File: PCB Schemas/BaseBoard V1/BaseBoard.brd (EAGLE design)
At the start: 94 x 31.1 mm, 31 parts, among them IC1 74HC595D, IC2 74HC595D, IC3 74HC595D, U1 ATMEGA2560AU, X1 16MHz

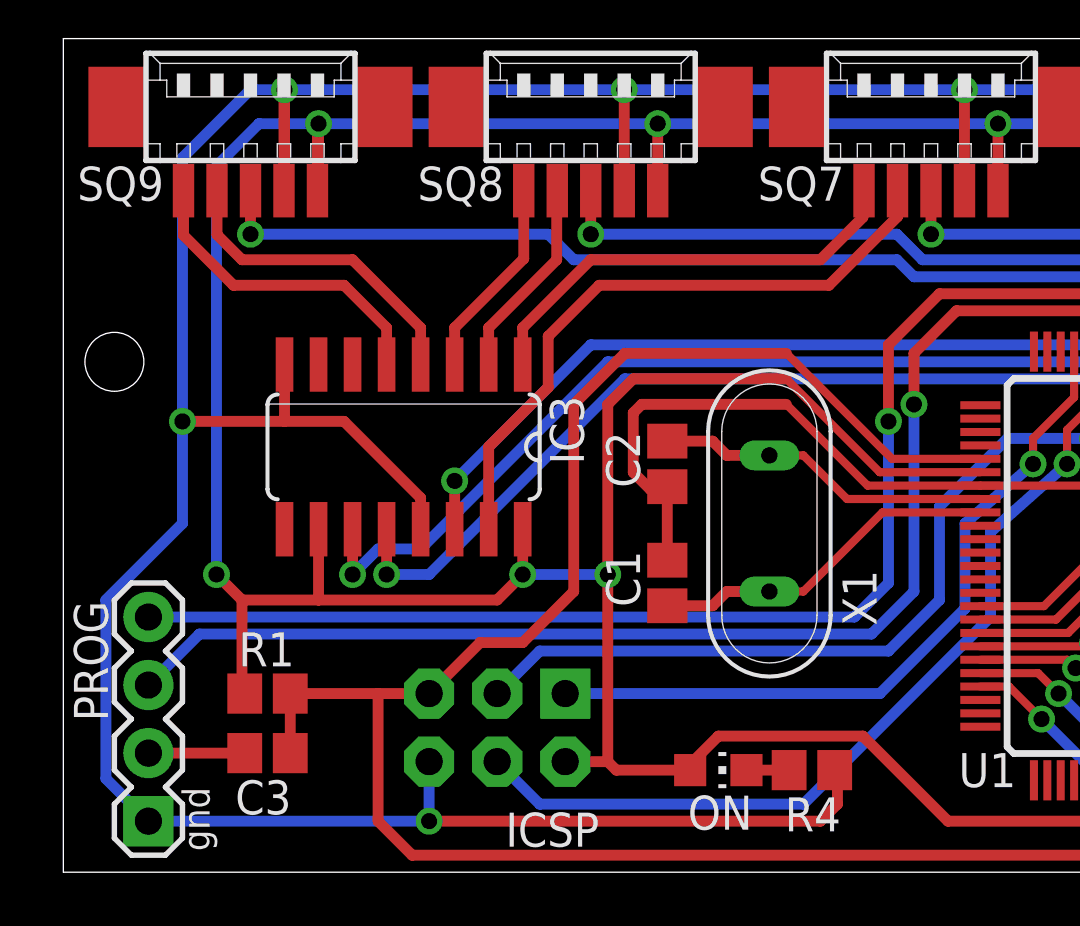
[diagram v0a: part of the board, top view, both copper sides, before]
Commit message: Corrected BaseBoard V1 and updated license file
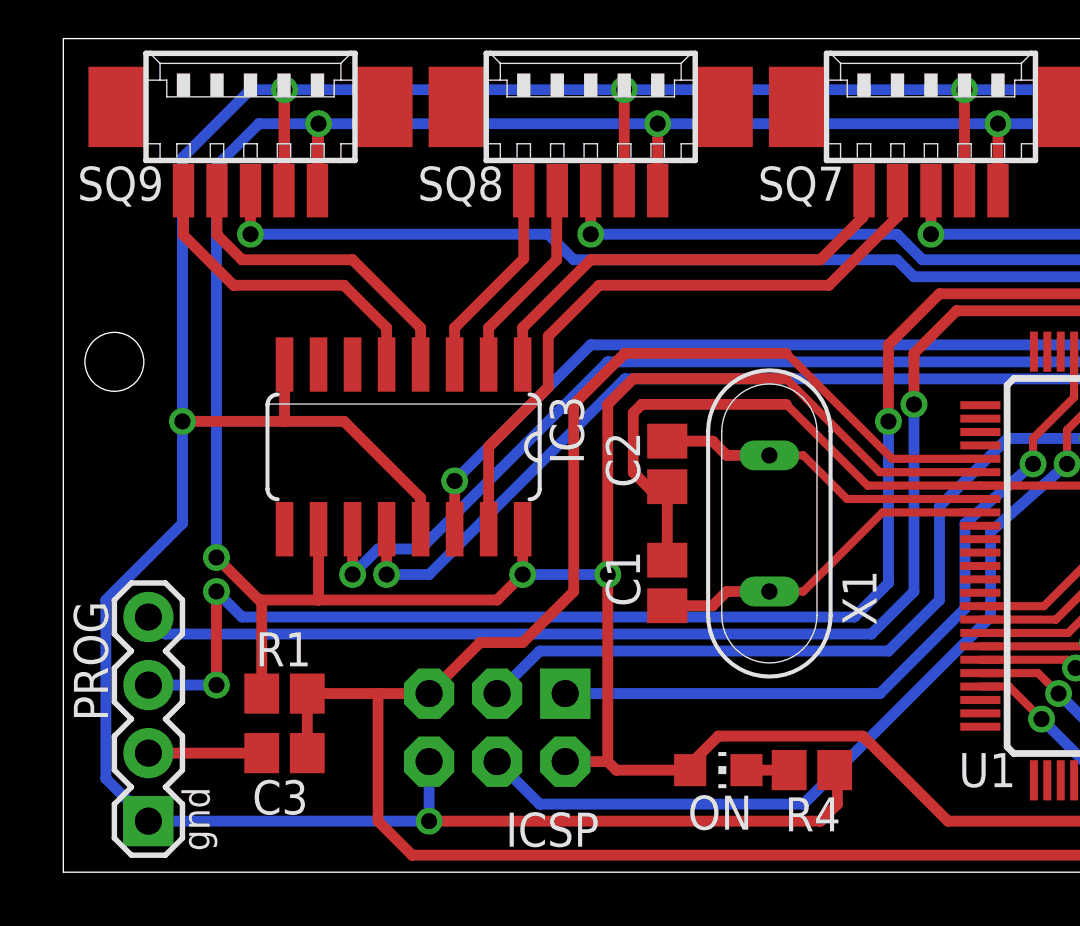
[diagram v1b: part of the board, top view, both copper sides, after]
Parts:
- moved C3 0.64 mm to (8.26, 4.45)
- moved R1 0.64 mm to (8.26, 6.67)
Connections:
- net RX: now also PROG.3; no longer PROG.4
- net TX: now also PROG.4; no longer PROG.3
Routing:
- net RX: track 56.5 -> 60.4 mm, vias 1 -> 3
- net RESET: track 100.3 -> 99.7 mm
- net N$5: track 3.59 -> 4.23 mm
- net TX: track 56.2 -> 55.7 mm
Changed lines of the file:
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@@
 <attribute name="VALUE" x="38.4175" y="16.51" size="0.4064" layer="27" rot="R270"/>
 </element>
-<element name="R1" library="resistor" package="R0805" value="10k" x="7.62" y="6.6675" smashed="yes" rot="R180">
-<attribute name="NAME" x="6.5405" y="7.6835" size="1.27" layer="25"/>
-<attribute name="VALUE" x="8.382" y="8.9535" size="1.27" layer="27" rot="R180"/>
+<element name="R1" library="resistor" package="R0805" value="10k" x="8.255" y="6.6675" smashed="yes" rot="R180">
+<attribute name="NAME" x="7.1755" y="7.6835" size="1.27" layer="25"/>
+<attribute name="VALUE" x="9.017" y="8.9535" size="1.27" layer="27" rot="R180"/>
 </element>
 <element name="X1" library="special" package="QS" value="16MHz" x="26.3525" y="13.0175" smashed="yes" rot="R90">
@@
 <attribute name="VALUE" x="6.35" y="0.635" size="1.27" layer="27" rot="R90"/>
 </element>
-<element name="C3" library="resistor" package="C0805" value="100nF" x="7.62" y="4.445" smashed="yes">
-<attribute name="NAME" x="8.509" y="3.429" size="1.27" layer="25" rot="R180"/>
-<attribute name="VALUE" x="6.731" y="2.159" size="1.27" layer="27"/>
+<element name="C3" library="resistor" package="C0805" value="100nF" x="8.255" y="4.445" smashed="yes">
+<attribute name="NAME" x="9.144" y="3.429" size="1.27" layer="25" rot="R180"/>
+<attribute name="VALUE" x="7.366" y="2.159" size="1.27" layer="27"/>
 </element>
 <element name="C4" library="resistor" package="C0805" value="100nF" x="54.2925" y="17.4625" rot="R270"/>
@@
 <via x="9.525" y="27.94" extent="1-16" drill="0.6"/>
 <wire x1="9.525" y1="27.94" x2="22.185" y2="27.94" width="0.4064" layer="16"/>
-<via x="5.715" y="11.1125" extent="1-16" drill="0.6"/>
-<wire x1="5.715" y1="11.1125" x2="5.715" y2="26.3525" width="0.4064" layer="16"/>
+<via x="5.715" y="11.7475" extent="1-16" drill="0.6"/>
+<wire x1="5.715" y1="11.7475" x2="5.715" y2="26.3525" width="0.4064" layer="16"/>
 <wire x1="5.715" y1="26.3525" x2="7.3025" y2="27.94" width="0.4064" layer="16"/>
 <wire x1="7.3025" y1="27.94" x2="9.525" y2="27.94" width="0.4064" layer="16"/>
 <wire x1="9.525" y1="10.16" x2="9.525" y2="12.8016" width="0.4064" layer="1"/>
-<wire x1="6.6675" y1="10.16" x2="9.525" y2="10.16" width="0.4064" layer="1"/>
-<wire x1="6.6675" y1="10.16" x2="6.6675" y2="6.77" width="0.4064" layer="1"/>
-<wire x1="6.6675" y1="6.77" x2="6.77" y2="6.6675" width="0.4064" layer="1"/>
 <wire x1="62.5475" y1="12.8016" x2="62.5475" y2="10.16" width="0.4064" layer="1"/>
 <wire x1="70.1675" y1="11.1125" x2="70.1675" y2="12.8016" width="0.4064" layer="1"/>
@@
 <wire x1="51.435" y1="17.78" x2="51.435" y2="20.0025" width="0.3048" layer="1"/>
 <wire x1="20.32" y1="4.1275" x2="18.7325" y2="4.1275" width="0.4064" layer="1"/>
-<wire x1="5.715" y1="11.1125" x2="6.6675" y2="10.16" width="0.4064" layer="1"/>
 <wire x1="9.525" y1="10.16" x2="16.1925" y2="10.16" width="0.4064" layer="1"/>
 <wire x1="17.145" y1="11.1125" x2="17.145" y2="12.8016" width="0.4064" layer="1"/>
@@
 <wire x1="71.04" y1="4.4925" x2="90.1775" y2="4.4925" width="0.4064" layer="16"/>
 <wire x1="90.1775" y1="4.4925" x2="90.805" y2="5.12" width="0.4064" layer="16"/>
+<wire x1="7.405" y1="6.6675" x2="7.405" y2="10.0575" width="0.4064" layer="1"/>
+<wire x1="7.405" y1="10.16" x2="7.405" y2="10.0575" width="0.4064" layer="1"/>
+<wire x1="7.405" y1="10.0575" x2="5.715" y2="11.7475" width="0.4064" layer="1"/>
+<wire x1="9.525" y1="10.16" x2="7.405" y2="10.16" width="0.4064" layer="1"/>
 </signal>
 <signal name="RESET">
@@
 <contactref element="C3" pad="2"/>
 <contactref element="ICSP" pad="5"/>
-<wire x1="8.47" y1="6.6675" x2="8.47" y2="4.445" width="0.4064" layer="1"/>
-<wire x1="8.47" y1="6.6675" x2="11.7475" y2="6.6675" width="0.4064" layer="1"/>
+<wire x1="9.105" y1="6.6675" x2="9.105" y2="4.445" width="0.4064" layer="1"/>
+<wire x1="9.105" y1="6.6675" x2="11.7475" y2="6.6675" width="0.4064" layer="1"/>
 <wire x1="11.7475" y1="6.6675" x2="13.6525" y2="6.6675" width="0.4064" layer="1"/>
 <wire x1="34.2275" y1="15.43" x2="30.925" y2="15.43" width="0.3048" layer="1"/>
@@
 </signal>
 <signal name="RX">
-<contactref element="PROG" pad="4"/>
 <contactref element="U1" pad="2"/>
 <wire x1="47.7275" y1="19.43" x2="47.7275" y2="20.8525" width="0.3048" layer="1"/>
@@
 <wire x1="46.99" y1="21.59" x2="32.7025" y2="21.59" width="0.4064" layer="1"/>
 <wire x1="32.7025" y1="21.59" x2="30.7975" y2="19.685" width="0.4064" layer="1"/>
-<wire x1="3.175" y1="9.525" x2="29.5275" y2="9.525" width="0.4064" layer="16"/>
-<wire x1="29.5275" y1="9.525" x2="30.7975" y2="10.795" width="0.4064" layer="16"/>
 <wire x1="30.7975" y1="10.795" x2="30.7975" y2="16.8275" width="0.4064" layer="16"/>
 <via x="30.7975" y="16.8275" extent="1-16" drill="0.6"/>
 <wire x1="30.7975" y1="19.685" x2="30.7975" y2="16.8275" width="0.4064" layer="1"/>
+<contactref element="PROG" pad="3"/>
+<wire x1="30.7975" y1="10.795" x2="29.5275" y2="9.525" width="0.4064" layer="16"/>
+<wire x1="29.5275" y1="9.525" x2="6.6675" y2="9.525" width="0.4064" layer="16"/>
+<wire x1="6.6675" y1="9.525" x2="5.715" y2="10.4775" width="0.4064" layer="16"/>
+<wire x1="3.175" y1="6.985" x2="5.715" y2="6.985" width="0.4064" layer="16"/>
+<via x="5.715" y="6.985" extent="1-16" drill="0.6"/>
+<via x="5.715" y="10.4775" extent="1-16" drill="0.6"/>
+<wire x1="5.715" y1="6.985" x2="5.715" y2="10.4775" width="0.4064" layer="1"/>
 </signal>
 <signal name="TX">
-<contactref element="PROG" pad="3"/>
 <contactref element="U1" pad="3"/>
 <wire x1="47.2275" y1="19.43" x2="47.2275" y2="20.4" width="0.3048" layer="1"/>
@@
 <wire x1="46.6725" y1="20.955" x2="33.3375" y2="20.955" width="0.4064" layer="1"/>
 <wire x1="33.3375" y1="20.955" x2="31.75" y2="19.3675" width="0.4064" layer="1"/>
-<wire x1="5.08" y1="8.89" x2="30.1625" y2="8.89" width="0.4064" layer="16"/>
-<wire x1="30.1625" y1="8.89" x2="31.75" y2="10.4775" width="0.4064" layer="16"/>
 <wire x1="31.75" y1="10.4775" x2="31.75" y2="17.4625" width="0.4064" layer="16"/>
 <via x="31.75" y="17.4625" extent="1-16" drill="0.6"/>
 <wire x1="31.75" y1="19.3675" x2="31.75" y2="17.4625" width="0.4064" layer="1"/>
-<wire x1="5.08" y1="8.89" x2="3.175" y2="6.985" width="0.4064" layer="16"/>
+<contactref element="PROG" pad="4"/>
+<wire x1="31.75" y1="10.4775" x2="30.1625" y2="8.89" width="0.4064" layer="16"/>
+<wire x1="30.1625" y1="8.89" x2="3.81" y2="8.89" width="0.4064" layer="16"/>
+<wire x1="3.81" y1="8.89" x2="3.175" y2="9.525" width="0.4064" layer="16"/>
 </signal>
 <signal name="N$5">
 <contactref element="PROG" pad="2"/>
 <contactref element="C3" pad="1"/>
-<wire x1="6.77" y1="4.445" x2="3.175" y2="4.445" width="0.4064" layer="1"/>
+<wire x1="7.405" y1="4.445" x2="3.175" y2="4.445" width="0.4064" layer="1"/>
 </signal>
 <signal name="AREF">

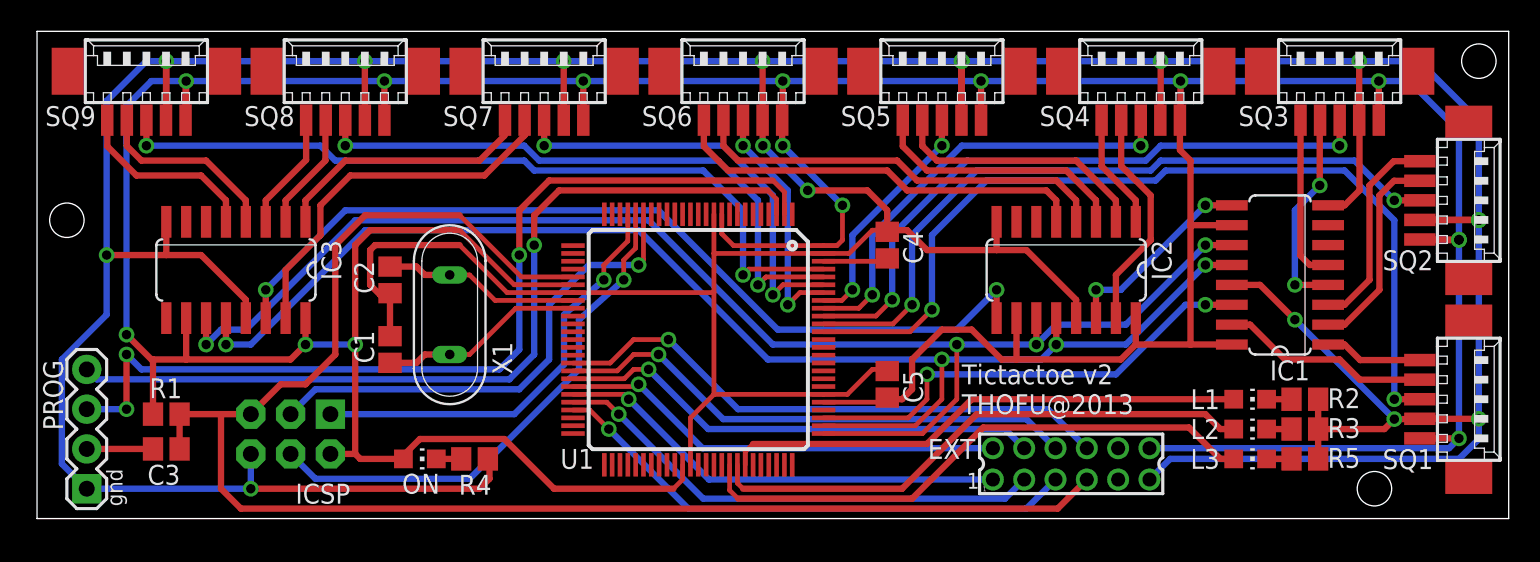
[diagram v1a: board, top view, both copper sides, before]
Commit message: Modified base conector; delete reset pin
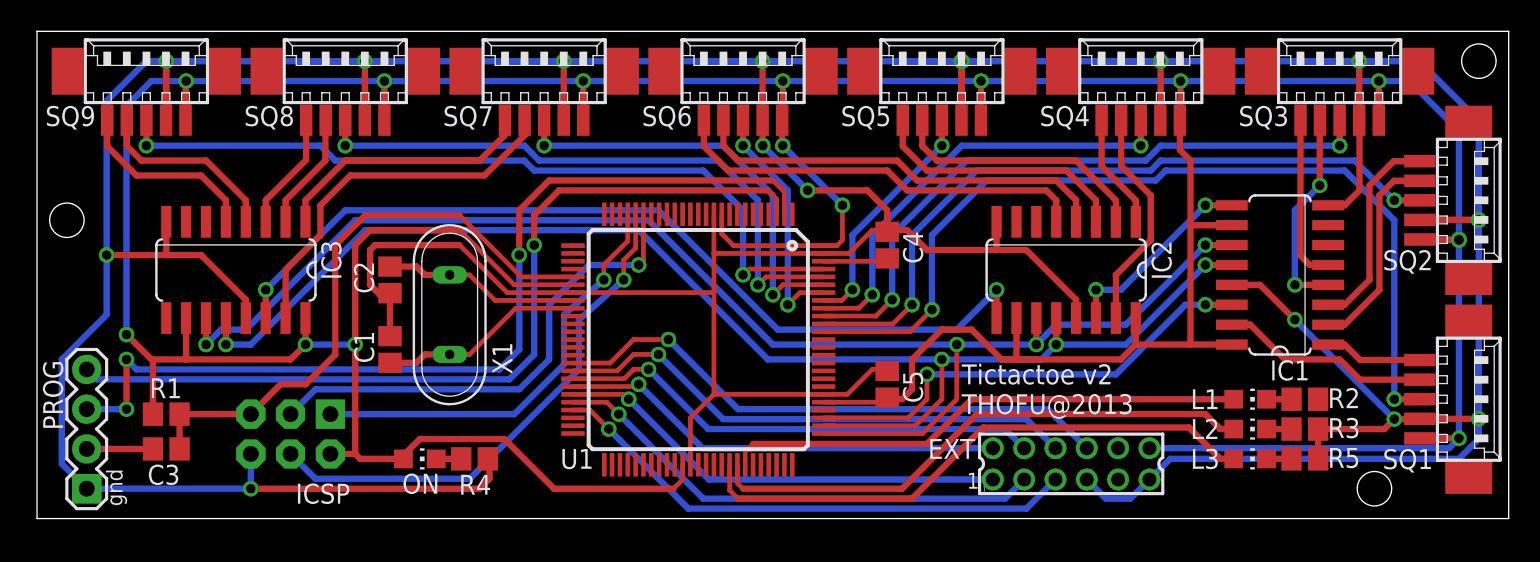
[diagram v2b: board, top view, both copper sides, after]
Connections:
- net DBG_G renamed DBG3
- net DBG_O renamed DBG1
- net DBG_R renamed DBG2
- net GND: now also EXT.7
- net RESET: no longer EXT.7
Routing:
- net RESET: track 99.7 -> 38.3 mm
- net GND: track 378.4 -> 381.5 mm
- net DBG3: track 33.4 -> 32.6 mm
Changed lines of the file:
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@@
 <wire x1="80.3275" y1="12.7" x2="86.6775" y2="6.35" width="0.4064" layer="16"/>
 <contactref element="EXT" pad="11"/>
-<contactref element="R2" pad="2"/>
 <contactref element="R3" pad="2"/>
 <wire x1="81.8125" y1="3.81" x2="81.8125" y2="5.715" width="0.4064" layer="1"/>
-<wire x1="81.8125" y1="5.715" x2="81.8125" y2="7.62" width="0.4064" layer="1"/>
 <wire x1="86.6775" y1="6.35" x2="86.0425" y2="5.715" width="0.4064" layer="1"/>
 <wire x1="86.0425" y1="5.715" x2="81.8125" y2="5.715" width="0.4064" layer="1"/>
@@
 <wire x1="28.8925" y1="2.54" x2="28.8925" y2="3.7075" width="0.4064" layer="1"/>
 <wire x1="28.8925" y1="3.7075" x2="28.79" y2="3.81" width="0.4064" layer="1"/>
+<contactref element="EXT" pad="7"/>
+<wire x1="67.04" y1="2.4925" x2="68.2625" y2="1.27" width="0.4064" layer="16"/>
+<wire x1="68.2625" y1="1.27" x2="69.8175" y2="1.27" width="0.4064" layer="16"/>
+<wire x1="69.8175" y1="1.27" x2="71.04" y2="2.4925" width="0.4064" layer="16"/>
+<contactref element="R2" pad="2"/>
+<wire x1="81.8125" y1="5.715" x2="81.8125" y2="7.62" width="0" layer="19" extent="1-1"/>
 </signal>
 <signal name="VCC">
@@
 <contactref element="U1" pad="30"/>
 <contactref element="R1" pad="1"/>
-<contactref element="C3" pad="2"/>
 <contactref element="ICSP" pad="5"/>
-<wire x1="9.105" y1="6.6675" x2="9.105" y2="4.445" width="0.4064" layer="1"/>
-<wire x1="9.105" y1="6.6675" x2="11.7475" y2="6.6675" width="0.4064" layer="1"/>
-<wire x1="11.7475" y1="6.6675" x2="13.6525" y2="6.6675" width="0.4064" layer="1"/>
 <wire x1="34.2275" y1="15.43" x2="30.925" y2="15.43" width="0.3048" layer="1"/>
 <wire x1="30.925" y1="15.43" x2="26.9875" y2="19.3675" width="0.3048" layer="1"/>
@@
 <wire x1="17.145" y1="8.5725" x2="15.5575" y2="8.5725" width="0.4064" layer="1"/>
 <wire x1="15.5575" y1="8.5725" x2="13.6525" y2="6.6675" width="0.4064" layer="1"/>
-<wire x1="65.1825" y1="0.635" x2="13.0175" y2="0.635" width="0.4064" layer="1"/>
-<wire x1="13.0175" y1="0.635" x2="11.7475" y2="1.905" width="0.4064" layer="1"/>
-<wire x1="11.7475" y1="1.905" x2="11.7475" y2="6.6675" width="0.4064" layer="1"/>
-<contactref element="EXT" pad="7"/>
-<wire x1="67.04" y1="2.4925" x2="65.1825" y2="0.635" width="0.4064" layer="1"/>
+<contactref element="C3" pad="2"/>
+<wire x1="9.105" y1="6.6675" x2="13.6525" y2="6.6675" width="0.4064" layer="1"/>
+<wire x1="9.105" y1="6.6675" x2="9.105" y2="4.445" width="0.4064" layer="1"/>
 </signal>
 <signal name="N$1">
@@
 <contactref element="PROG" pad="3"/>
 <wire x1="30.7975" y1="10.795" x2="29.5275" y2="9.525" width="0.4064" layer="16"/>
-<wire x1="29.5275" y1="9.525" x2="6.6675" y2="9.525" width="0.4064" layer="16"/>
-<wire x1="6.6675" y1="9.525" x2="5.715" y2="10.4775" width="0.4064" layer="16"/>
+<wire x1="29.5275" y1="9.525" x2="6.35" y2="9.525" width="0.4064" layer="16"/>
+<wire x1="6.35" y1="9.525" x2="5.715" y2="10.16" width="0.4064" layer="16"/>
 <wire x1="3.175" y1="6.985" x2="5.715" y2="6.985" width="0.4064" layer="16"/>
 <via x="5.715" y="6.985" extent="1-16" drill="0.6"/>
-<via x="5.715" y="10.4775" extent="1-16" drill="0.6"/>
-<wire x1="5.715" y1="6.985" x2="5.715" y2="10.4775" width="0.4064" layer="1"/>
+<via x="5.715" y="10.16" extent="1-16" drill="0.6"/>
+<wire x1="5.715" y1="6.985" x2="5.715" y2="10.16" width="0.4064" layer="1"/>
 </signal>
 <signal name="TX">
@@
 <wire x1="78.52" y1="3.81" x2="80.1125" y2="3.81" width="0.4064" layer="1"/>
 </signal>
-<signal name="DBG_R">
+<signal name="DBG2">
 <contactref element="L2" pad="A"/>
 <contactref element="U1" pad="68"/>
@@
 <wire x1="75.565" y1="5.715" x2="76.42" y2="5.715" width="0.4064" layer="1"/>
 </signal>
-<signal name="DBG_G">
+<signal name="DBG3">
 <contactref element="L1" pad="A"/>
-<contactref element="U1" pad="69"/>
 <wire x1="59.69" y1="7.62" x2="76.42" y2="7.62" width="0.4064" layer="1"/>
-<wire x1="45.2275" y1="3.43" x2="45.2275" y2="4.27" width="0.3048" layer="1"/>
 <wire x1="45.2275" y1="4.27" x2="45.72" y2="4.7625" width="0.3048" layer="1"/>
 <wire x1="45.72" y1="4.7625" x2="56.8325" y2="4.7625" width="0.4064" layer="1"/>
 <wire x1="56.8325" y1="4.7625" x2="59.69" y2="7.62" width="0.4064" layer="1"/>
+<contactref element="U1" pad="69"/>
+<wire x1="45.2275" y1="3.43" x2="45.2275" y2="4.27" width="0" layer="19" extent="1-1"/>
 </signal>
 <signal name="RED4">
@@
 <contactref element="EXT" pad="9"/>
 </signal>
-<signal name="DBG_O">
+<signal name="DBG1">
 <contactref element="L3" pad="A"/>
 <contactref element="U1" pad="67"/>
